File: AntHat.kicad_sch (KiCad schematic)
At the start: 37 parts, among them J1 Raspberry_Pi_2_3, J2 0455580003, Q1 DMP3013SFV-7, U1 AP64501SP-13

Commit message: finished routing. added logo
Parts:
- added C20: 0.1uF, Capacitor_SMD:C_0402_1005Metric, symbol Device:C
- added J10, J11, J8, J9: 0353180420, AntHat:MOLEX_353180420, symbol Connector_Generic:Conn_02x02_Counter_Clockwise
- added J3: PSU Comm, AntHat:CONN-TH_6P-P2.00_PHD-2X3A, symbol Connector_Generic:Conn_02x03_Odd_Even
- added J4, J5, J6, J7: 61900411021, AntHat:CONN_61900411021_WRE, symbol Connector_Generic:Conn_01x04
- added R10, R11, R12, R9: 36K, Resistor_SMD:R_0402_1005Metric, symbol Device:R_US
- added R13, R14, R15, R16: 10k, Resistor_SMD:R_0402_1005Metric, symbol Device:R_US
- added R17, R18, R6: 4.7k, Resistor_SMD:R_0402_1005Metric, symbol Device:R_US
- added R7: 33k, Resistor_SMD:R_0402_1005Metric, symbol Device:R_US
- added R8: 22k, Resistor_SMD:R_0402_1005Metric, symbol Device:R_US
- added U2: EMC2305, AntHat:QFN16_4x4MC_MCH, symbol AntHat:EMC2305-1-AP-TR
- C10, C8, C9: DK 478-KGM05AR71C104KHCT-ND -> (none); PARTNO KGM05AR71C104KH -> (none)
- D1: footprint bitcart:D_SOT-23_ANK -> AntHat:D_SOT-23_ANK
- J1: footprint pihat:ESQ-120-14-T-D -> AntHat:ESQ-120-14-T-D; symbol pihat-rescue:Raspberry_Pi_2_3-Connector -> AntHat:Raspberry_Pi_2_3-Connector
- J2: footprint bitcart:0455580003 -> AntHat:0455580003; symbol bitcart:0455580003 -> AntHat:0455580003
- U1: symbol CM4IO:AP64351 -> AntHat:AP64351
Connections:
- net 12V: now also J10.2 (Pin_2), J11.2 (Pin_2), J4.2 (Pin_2), J5.2 (Pin_2), J6.2 (Pin_2), J7.2 (Pin_2), J8.2 (Pin_2), J9.2 (Pin_2)
- net 5V: now also R13.1, R14.1, R15.1, R16.1
- net GND: now also C20.2, J10.1 (Pin_1), J11.1 (Pin_1), J3.2 (Pin_2), J4.1 (Pin_1), J5.1 (Pin_1), J6.1 (Pin_1), J7.1 (Pin_1), J8.1 (Pin_1), J9.1 (Pin_1), U2.17 (GND)
- net VIN: now reaches C5.1, J2.1, J2.2, J2.3, Q1.5 (D)
- net +3.3v: now reaches J1.1 (3V3)
- net +3.3v: now also J1.17 (3V3), C20.1, R10.1, R11.1, R12.1, R17.2, R18.2, R6.2, R7.2, R8.2, R9.1, U2.3 (VDD)
- net PSU_EN: now reaches J1.11 (GPIO17)
- net PSU_EN: now also J3.5 (Pin_5)
- net SDA: now reaches J1.3 (SDA/GPIO2)
- net SDA: now also J3.3 (Pin_3), R17.1, U2.1 (SMDATA)
- net FAN_ALERT: now reaches J1.36 (GPIO16)
- net FAN_ALERT: now also R6.1, U2.12 (~{ALERT})
- net SCL: now reaches J1.5 (SCL/GPIO3)
- net SCL: now also J3.6 (Pin_6), R18.1, U2.2 (SMCLK)
- new net: R7.1, U2.4 (ADDR_SEL)
- new net: R8.1, U2.11 (CLK)
- new net PWM1: J4.4 (Pin_4), J8.4 (Pin_4), R13.2, U2.5 (PWM1)
- new net PWM2: J5.4 (Pin_4), J9.4 (Pin_4), R14.2, U2.7 (PWM2)
- new net PWM3: J10.4 (Pin_4), J6.4 (Pin_4), R15.2, U2.9 (PWM3)
- new net PWM4: J11.4 (Pin_4), J7.4 (Pin_4), R16.2, U2.13 (PWM4)
- new net TACH1: J4.3 (Pin_3), J8.3 (Pin_3), R9.2, U2.6 (TACH1)
- new net TACH2: J5.3 (Pin_3), J9.3 (Pin_3), R10.2, U2.8 (TACH2)
- new net TACH3: J10.3 (Pin_3), J6.3 (Pin_3), R11.2, U2.10 (TACH3)
- new net TACH4: J11.3 (Pin_3), J7.3 (Pin_3), R12.2, U2.14 (TACH4)
- no-connect marks 0 -> 2
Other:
- note added: "FAN controller"
- note added: "Fans"
- title: (none) -> AntHat
- moved on the sheet: C1, C10, C11, C12, C13, C14, C15, C16, C17, C18, C19, C2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

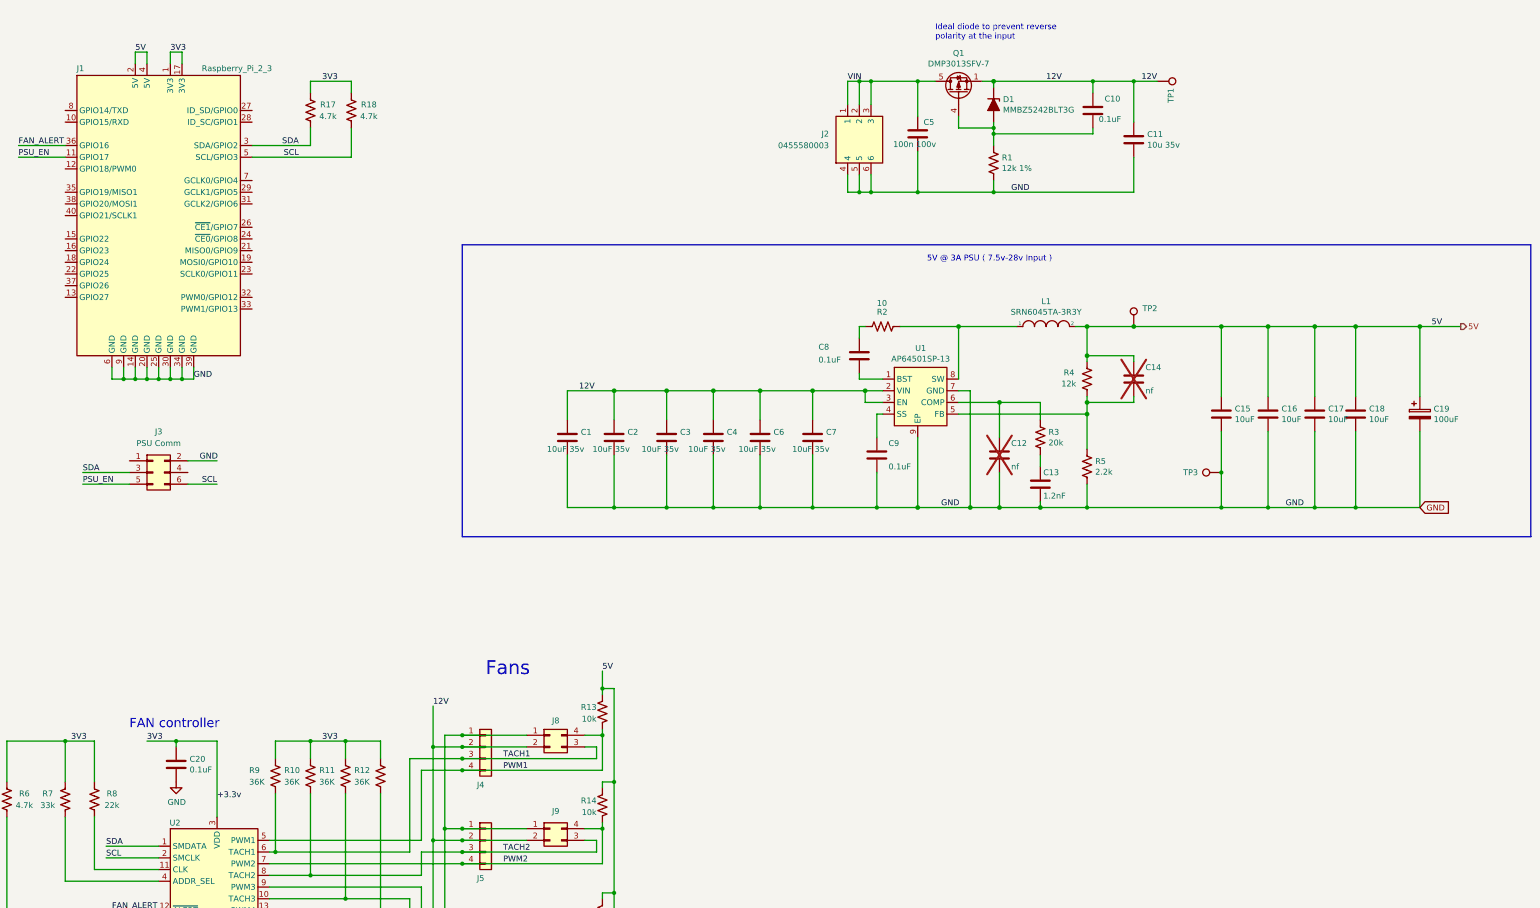
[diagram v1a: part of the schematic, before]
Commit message: added the TPS54531 since the AP64501SP-13 isn't on DK. prolly will delete
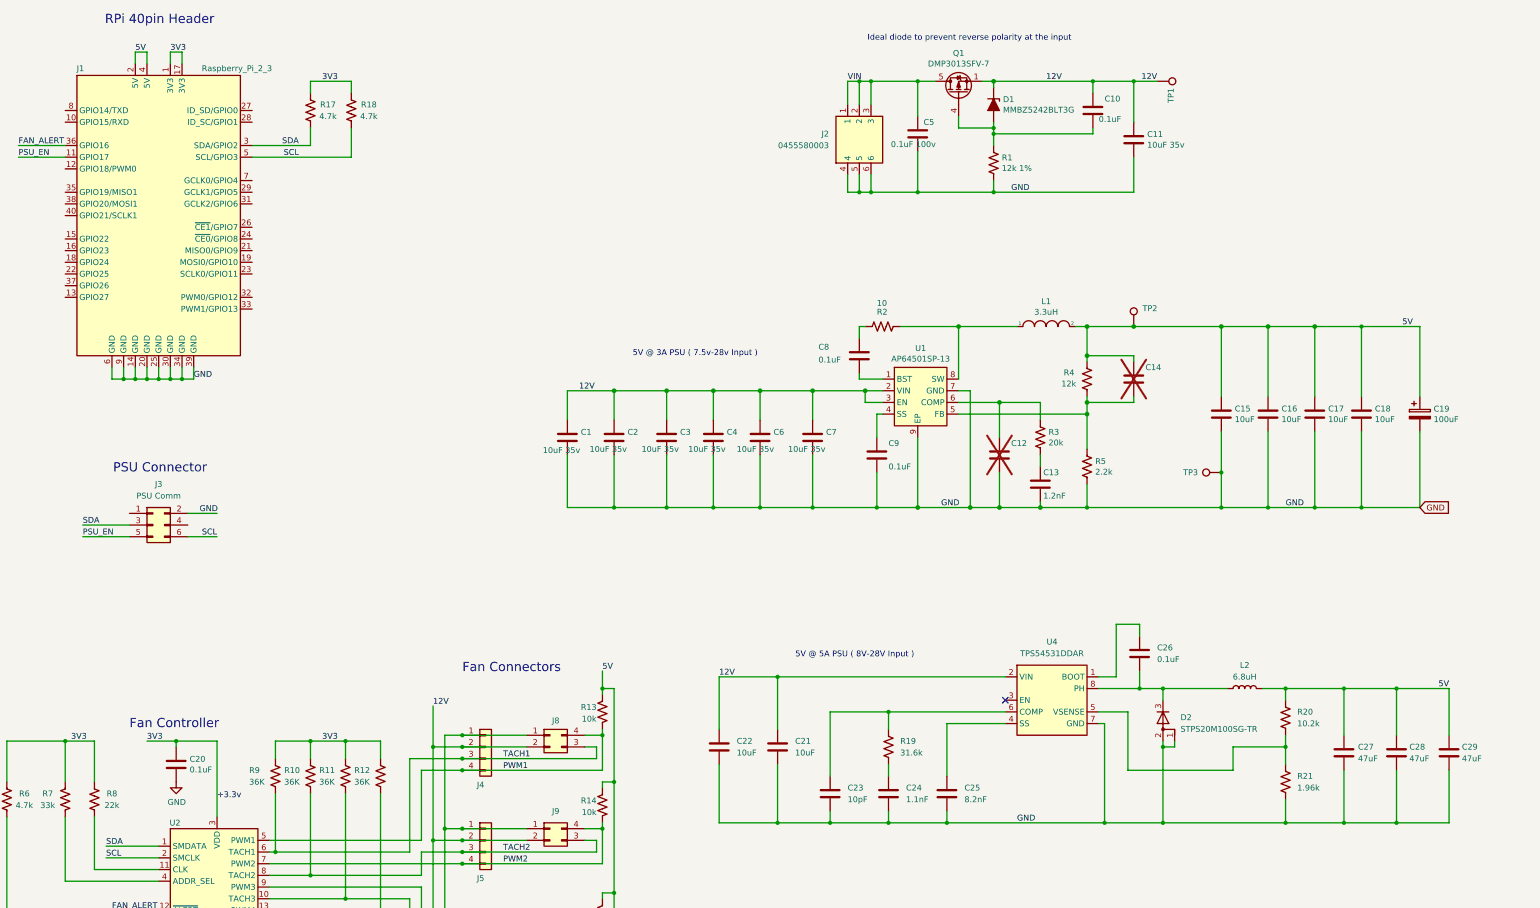
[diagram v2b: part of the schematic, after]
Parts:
- added C21, C22: 10uF, Capacitor_SMD:C_1210_3225Metric, symbol Device:C
- added C23: 10pF, Capacitor_SMD:C_0805_2012Metric, symbol Device:C
- added C24: 1.1nF, Capacitor_SMD:C_0402_1005Metric, symbol Device:C
- added C25: 8.2nF, Capacitor_SMD:C_0402_1005Metric, symbol Device:C
- added C26: 0.1uF, Capacitor_SMD:C_0402_1005Metric, symbol Device:C
- added C27, C28, C29: 47uF, Capacitor_SMD:C_1210_3225Metric, symbol Device:C
- added D2: STPS20M100SG-TR, AntHat:D2PAK_L10.4-W8.5-P2.54-LS15.4-BR, symbol Device:D_AAK
- added L2: 6.8uH, AntHat:IND_IHLP-4040DZ_VIS, symbol Device:L
- added R19: 31.6k, Resistor_SMD:R_0402_1005Metric, symbol Device:R_US
- added R20: 10.2k, Resistor_SMD:R_0402_1005Metric, symbol Device:R_US
- added R21: 1.96k, Resistor_SMD:R_0402_1005Metric, symbol Device:R_US
- added U4: TPS54531DDAR, AntHat:SOIC-8_L5.0-W4.0-P1.27-LS6.0-BL-EP2.0, symbol AntHat:TPS54531DDAR
- C11: value 10u 35v -> 10uF 35v
- C12, C14: value nf -> ~
- C5: value 100n 100v -> 0.1uF 100v
- J1: LCSC Part (none) -> C2977589
- J2: LCSC Part (none) -> C19188571
- J3: LCSC Part (none) -> C2845614
- L1: value SRN6045TA-3R3Y -> 3.3uH
- Q1: LCSC Part (none) -> C264098
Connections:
- net 12V: now also C21.1, C22.1, U4.2 (VIN)
- net 5V: now also C27.1, C28.1, C29.1, L2.2, R20.1
- net GND: now also C21.2, C22.2, C23.2, C24.2, C25.2, C27.2, C28.2, C29.2, D2.1 (A), D2.2 (A), R21.2, U4.7 (GND), U4.9 (EP)
- new net: C26.1, U4.1 (BOOT)
- new net: C25.1, U4.4 (SS)
- new net: R20.2, R21.1, U4.5 (VSENSE)
- new net: C23.1, R19.1, U4.6 (COMP)
- new net: C26.2, D2.3 (K), L2.1, U4.8 (PH)
- new net: C24.1, R19.2
- no-connect marks 2 -> 3
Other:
- note added: "5V @ 5A PSU ( 8V-28V Input )"
- note added: "Fan Connectors"
- note added: "Fan Controller"
- note added: "PSU Connector"
- note added: "RPi 40pin Header"
- note removed: "FAN controller"
- note removed: "Fans"
- moved on the sheet: C18, J3
